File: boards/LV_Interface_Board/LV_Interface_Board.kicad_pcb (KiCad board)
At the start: 2 copper layers, 136 x 100 mm, 23 parts, among them J1 Ampseal_35, J2 Ampseal_35, J3 micromatch_male_6, J4 micromatch_male_20, J5 micromatch_male_20, J6 micromatch_male_12, J7 micromatch_male_18, J8 micromatch_male_20, J9 micromatch_male_20, SW1 3P4T_rotary_switch, U1 RJ45_VT, U2 HT16K33

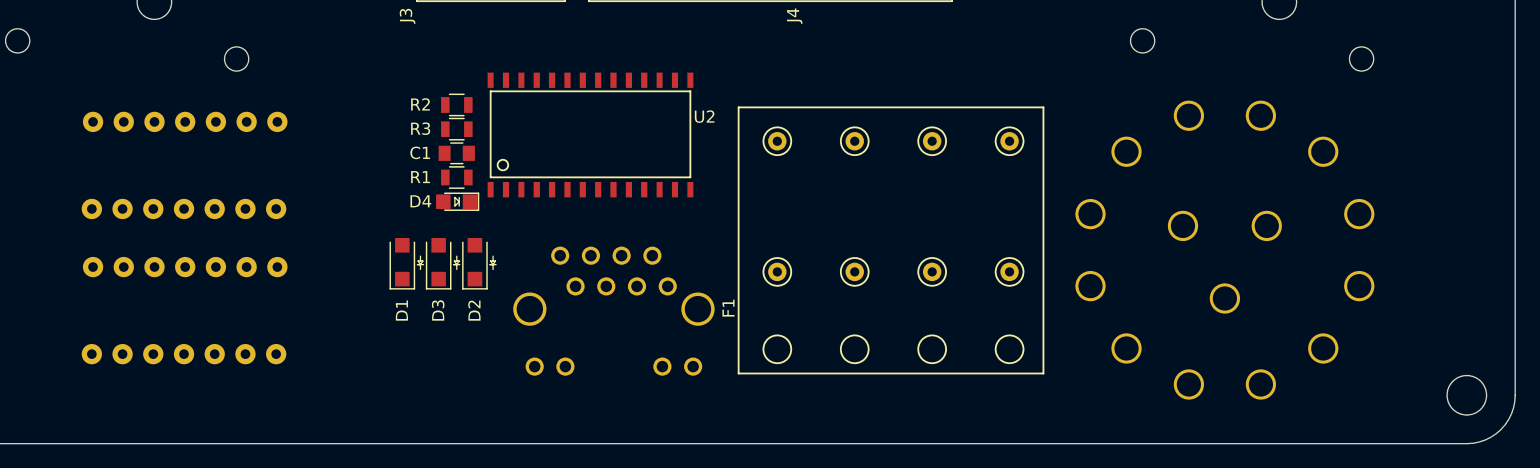
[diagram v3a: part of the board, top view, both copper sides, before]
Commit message: updated layout based on CAD interferences
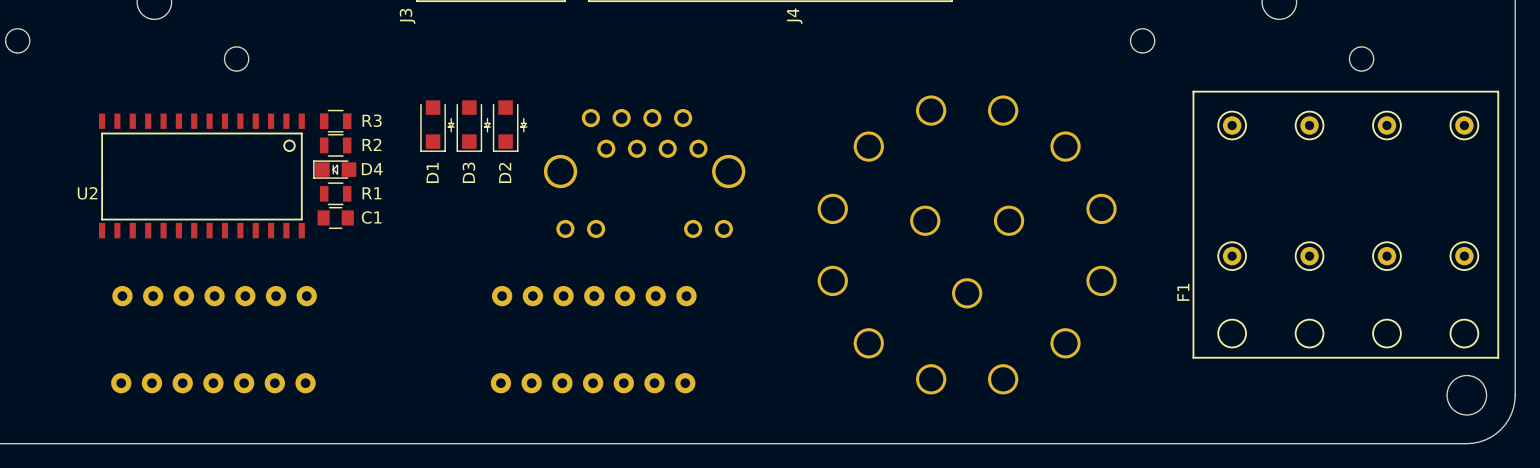
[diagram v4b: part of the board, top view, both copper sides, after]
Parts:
- moved F1 37.6 mm to (139.6, 140.9)
- moved LED1 33.9 mm to (86.8, 141.4)
- moved SW1 21.3 mm to (117.7, 133.6)
- moved U2 16.6 mm to (62.7, 123.3), turned to 180 degrees
- moved LED2 14.6 mm to (55.4, 141.4)
- moved D1 11.7 mm to (73.5, 123.6)
- moved D2 11.7 mm to (79.5, 123.6)
- moved D3 11.7 mm to (76.5, 123.6)
- moved U1 11.7 mm to (97.6, 132.3)
- moved C1 11.3 mm to (65.5, 131.3), turned to 180 degrees
- moved R2 10.6 mm to (65.5, 125.3), turned to 180 degrees
- moved D4 10.4 mm to (65.5, 127.3), turned to 0 degrees
- moved R1 10.1 mm to (65.5, 129.3), turned to 180 degrees
- moved R3 10.0 mm to (65.5, 123.3), turned to 180 degrees

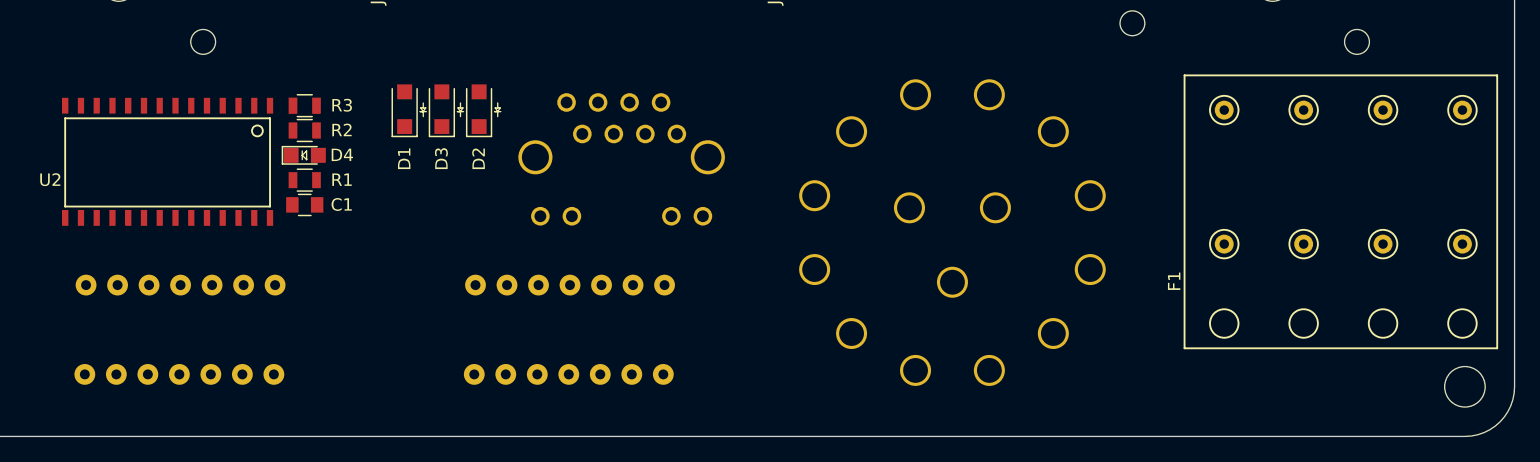
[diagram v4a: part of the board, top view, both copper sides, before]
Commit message: finished CAD, fixed fuse block footprint
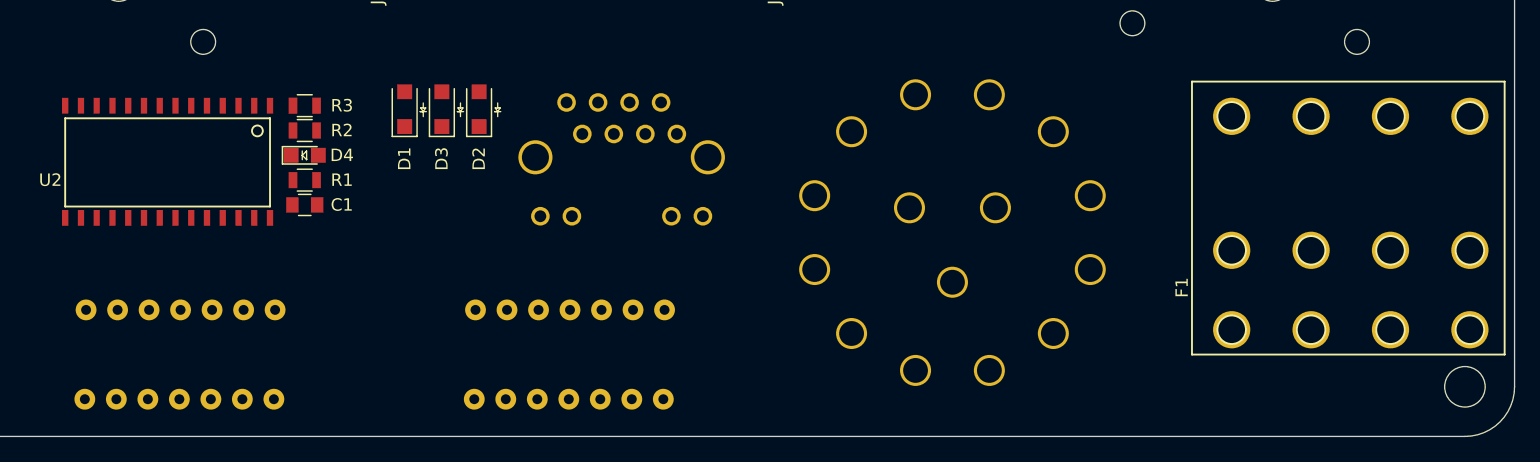
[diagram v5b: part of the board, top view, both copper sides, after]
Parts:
- moved LED1 2.00 mm to (86.8, 143.4)
- moved LED2 2.00 mm to (55.4, 143.4)
- moved F1 0.78 mm to (140.2, 141.4)
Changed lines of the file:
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@@
     (links 173)
     (no_connects 173)
-    (area 6.435716 32.3 178.564286 172.0894)
+    (area 26.949999 49.949999 163.050001 150.050001)
     (thickness 1.6)
     (drawings 34)
@@
     )
   )
-  (module footprints:fuse_block (layer F.Cu)
-    (at 139.6 140.898 90)
-    (fp_text reference F1 (at 3.4 -4 90) (layer F.SilkS)
-      (effects (font (size 1 1) (thickness 0.15)))
-    )
-    (fp_text value fuse_holder_125V_15A (at 4.4 -5.8 90) (layer F.Fab)
-      (effects (font (size 1 1) (thickness 0.15)))
-    )
-    (fp_line (start -2 22) (end -2 -3.2) (layer F.SilkS) (width 0.15))
-    (fp_line (start 20 22) (end -2 22) (layer F.SilkS) (width 0.15))
-    (fp_line (start 20 -3.2) (end 20 22) (layer F.SilkS) (width 0.15))
-    (fp_line (start -2 -3.2) (end 20 -3.2) (layer F.SilkS) (width 0.15))
-    (fp_circle (center 17.2 19.2) (end 16.05 19.2) (layer F.SilkS) (width 0.15))
-    (fp_circle (center 17.2 12.8) (end 16.05 12.8) (layer F.SilkS) (width 0.15))
-    (fp_circle (center 17.2 6.4) (end 16.05 6.4) (layer F.SilkS) (width 0.15))
-    (fp_circle (center 6.4 19.2) (end 5.25 19.2) (layer F.SilkS) (width 0.15))
-    (fp_circle (center 6.4 12.8) (end 5.25 12.8) (layer F.SilkS) (width 0.15))
-    (fp_circle (center 6.4 6.4) (end 6.4 5.25) (layer F.SilkS) (width 0.15))
-    (fp_circle (center 0 19.2) (end 0 18.05) (layer F.SilkS) (width 0.15))
-    (fp_circle (center 0 12.8) (end 0 11.65) (layer F.SilkS) (width 0.15))
-    (fp_circle (center 0 6.4) (end 0 5.25) (layer F.SilkS) (width 0.15))
-    (fp_circle (center 17.2 0) (end 16.05 0) (layer F.SilkS) (width 0.15))
-    (fp_circle (center 6.4 0) (end 5.25 0) (layer F.SilkS) (width 0.15))
-    (fp_circle (center 0 0) (end 0 1.15) (layer F.SilkS) (width 0.15))
-    (pad 1 thru_hole circle (at 6.4 0 90) (size 1.524 1.524) (drill 0.762) (layers *.Cu *.Mask F.SilkS)
-      (net 7 /GLVMS))
-    (pad 2 thru_hole circle (at 17.2 0 90) (size 1.524 1.524) (drill 0.762) (layers *.Cu *.Mask F.SilkS)
-      (net 8 /12V))
-    (pad 3 thru_hole circle (at 6.4 6.4 90) (size 1.524 1.524) (drill 0.762) (layers *.Cu *.Mask F.SilkS)
-      (net 7 /GLVMS))
-    (pad 4 thru_hole circle (at 17.2 6.4 90) (size 1.524 1.524) (drill 0.762) (layers *.Cu *.Mask F.SilkS)
-      (net 9 /COOLING_PUMP_12V_FUSED))
-    (pad 5 thru_hole circle (at 6.4 12.8 90) (size 1.524 1.524) (drill 0.762) (layers *.Cu *.Mask F.SilkS)
-      (net 7 /GLVMS))
-    (pad 6 thru_hole circle (at 17.2 12.8 90) (size 1.524 1.524) (drill 0.762) (layers *.Cu *.Mask F.SilkS)
-      (net 10 /MAIN_SHUTDOWN_FUSE))
-    (pad 7 thru_hole circle (at 6.4 19.2 90) (size 1.524 1.524) (drill 0.762) (layers *.Cu *.Mask F.SilkS)
-      (net 11 "Net-(F1-Pad7)"))
-    (pad 8 thru_hole circle (at 17.2 19.2 90) (size 1.524 1.524) (drill 0.762) (layers *.Cu *.Mask F.SilkS)
-      (net 12 "Net-(F1-Pad8)"))
-    (model /home/lucky/Desktop/Formula/OEM_Preferred_Parts/3DModels/fuse_block/fuse_block.wrl
-      (at (xyz 0 0 0))
-      (scale (xyz 1 1 1))
-      (rotate (xyz 0 0 0))
-    )
-  )
   (module footprints:Ampseal_35 (layer B.Cu)
     (at 143.5 56.5 270)
@@
     (pad 28 smd rect (at 0 -9.0424 180) (size 0.508 1.27) (layers F.Cu F.Paste F.Mask)
       (net 1 /5V))
+    (model /home/lucky/Desktop/Formula/OEM_Preferred_Parts/3DModels/SOP28/Document_sp.wrl
+      (at (xyz 0 0 0))
+      (scale (xyz 1 1 1))
+      (rotate (xyz 0 0 0))
+    )
   )
   (module footprints:SEGMENT_BICOL_BL-AR12Z3010 (layer B.Cu)
-    (at 86.81974 141.40082 270)
+    (at 86.81974 143.40082 270)
     (descr "SOUCE: HTTP://WWW.BETLUX.COM/PRODUCT/LED_LIGHT_BAR/BL-AR12B3010XX.PDF")
     (tags "SOUCE: HTTP://WWW.BETLUX.COM/PRODUCT/LED_LIGHT_BAR/BL-AR12B3010XX.PDF")
@@
     (pad 14 thru_hole circle (at 3.59918 7.66826 270) (size 1.6764 1.6764) (drill 0.79756) (layers *.Cu *.Paste *.Mask)
       (net 93 /COM0))
+    (model /home/lucky/Desktop/Formula/OEM_Preferred_Parts/3DModels/SEGMENT_BICOL_BL-AR12Z3010/led_bar.wrl
+      (at (xyz 0 0 0))
+      (scale (xyz 1 1 1))
+      (rotate (xyz 0 0 0))
+    )
   )
   (module footprints:SEGMENT_BICOL_BL-AR12Z3010 (layer B.Cu)
-    (at 55.4308 141.40082 270)
+    (at 55.4308 143.40082 270)
     (descr "SOUCE: HTTP://WWW.BETLUX.COM/PRODUCT/LED_LIGHT_BAR/BL-AR12B3010XX.PDF")
     (tags "SOUCE: HTTP://WWW.BETLUX.COM/PRODUCT/LED_LIGHT_BAR/BL-AR12B3010XX.PDF")
@@
     (pad 14 thru_hole circle (at 3.59918 7.66826 270) (size 1.6764 1.6764) (drill 0.79756) (layers *.Cu *.Paste *.Mask)
       (net 93 /COM0))
+    (model /home/lucky/Desktop/Formula/OEM_Preferred_Parts/3DModels/SEGMENT_BICOL_BL-AR12Z3010/led_bar.wrl
+      (at (xyz 0 0 0))
+      (scale (xyz 1 1 1))
+      (rotate (xyz 0 0 0))
+    )
+  )
+  (module footprints:fuse_block (layer F.Cu)
+    (at 140.2 141.4 90)
+    (fp_text reference F1 (at 3.4 -4 90) (layer F.SilkS)
+      (effects (font (size 1 1) (thickness 0.15)))
+    )
+    (fp_text value fuse_holder_125V_15A (at 4.4 -5.8 90) (layer F.Fab)
+      (effects (font (size 1 1) (thickness 0.15)))
+    )
+    (fp_line (start -2 22) (end -2 -3.2) (layer F.SilkS) (width 0.15))
+    (fp_line (start 20 22) (end -2 22) (layer F.SilkS) (width 0.15))
+    (fp_line (start 20 -3.2) (end 20 22) (layer F.SilkS) (width 0.15))
+    (fp_line (start -2 -3.2) (end 20 -3.2) (layer F.SilkS) (width 0.15))
+    (fp_circle (center 17.2 19.2) (end 16.05 19.2) (layer F.SilkS) (width 0.15))
+    (fp_circle (center 17.2 12.8) (end 16.05 12.8) (layer F.SilkS) (width 0.15))
+    (fp_circle (center 17.2 6.4) (end 16.05 6.4) (layer F.SilkS) (width 0.15))
+    (fp_circle (center 6.4 19.2) (end 5.25 19.2) (layer F.SilkS) (width 0.15))
+    (fp_circle (center 6.4 12.8) (end 5.25 12.8) (layer F.SilkS) (width 0.15))
+    (fp_circle (center 6.4 6.4) (end 6.4 5.25) (layer F.SilkS) (width 0.15))
+    (fp_circle (center 0 19.2) (end 0 18.05) (layer F.SilkS) (width 0.15))
+    (fp_circle (center 0 12.8) (end 0 11.65) (layer F.SilkS) (width 0.15))
+    (fp_circle (center 0 6.4) (end 0 5.25) (layer F.SilkS) (width 0.15))
+    (fp_circle (center 17.2 0) (end 16.05 0) (layer F.SilkS) (width 0.15))
+    (fp_circle (center 6.4 0) (end 5.25 0) (layer F.SilkS) (width 0.15))
+    (fp_circle (center 0 0) (end 0 1.15) (layer F.SilkS) (width 0.15))
+    (pad 1 thru_hole circle (at 6.4 0 90) (size 3 3) (drill 2.3) (layers *.Cu *.Mask F.SilkS)
+      (net 7 /GLVMS))
+    (pad 2 thru_hole circle (at 17.2 0 90) (size 3 3) (drill 2.3) (layers *.Cu *.Mask F.SilkS)
+      (net 8 /12V))
+    (pad 3 thru_hole circle (at 6.4 6.4 90) (size 3 3) (drill 2.3) (layers *.Cu *.Mask F.SilkS)
+      (net 7 /GLVMS))
+    (pad 4 thru_hole circle (at 17.2 6.4 90) (size 3 3) (drill 2.3) (layers *.Cu *.Mask F.SilkS)
+      (net 9 /COOLING_PUMP_12V_FUSED))
+    (pad 5 thru_hole circle (at 6.4 12.8 90) (size 3 3) (drill 2.3) (layers *.Cu *.Mask F.SilkS)
+      (net 7 /GLVMS))
+    (pad 6 thru_hole circle (at 17.2 12.8 90) (size 3 3) (drill 2.3) (layers *.Cu *.Mask F.SilkS)
+      (net 10 /MAIN_SHUTDOWN_FUSE))
+    (pad 7 thru_hole circle (at 6.4 19.2 90) (size 3 3) (drill 2.3) (layers *.Cu *.Mask F.SilkS)
+      (net 11 "Net-(F1-Pad7)"))
+    (pad 8 thru_hole circle (at 17.2 19.2 90) (size 3 3) (drill 2.3) (layers *.Cu *.Mask F.SilkS)
+      (net 12 "Net-(F1-Pad8)"))
+    (pad 9 thru_hole circle (at 0 0 90) (size 3 3) (drill 2.3) (layers *.Cu *.Mask F.SilkS))
+    (pad 10 thru_hole circle (at 0 6.4 90) (size 3 3) (drill 2.3) (layers *.Cu *.Mask F.SilkS))
+    (pad 11 thru_hole circle (at 0 12.8 90) (size 3 3) (drill 2.3) (layers *.Cu *.Mask F.SilkS))
+    (pad 12 thru_hole circle (at 0 19.2 90) (size 3 3) (drill 2.3) (layers *.Cu *.Mask F.SilkS))
   )
   (gr_circle (center 31 146) (end 32.63195 146) (layer Edge.Cuts) (width 0.1))

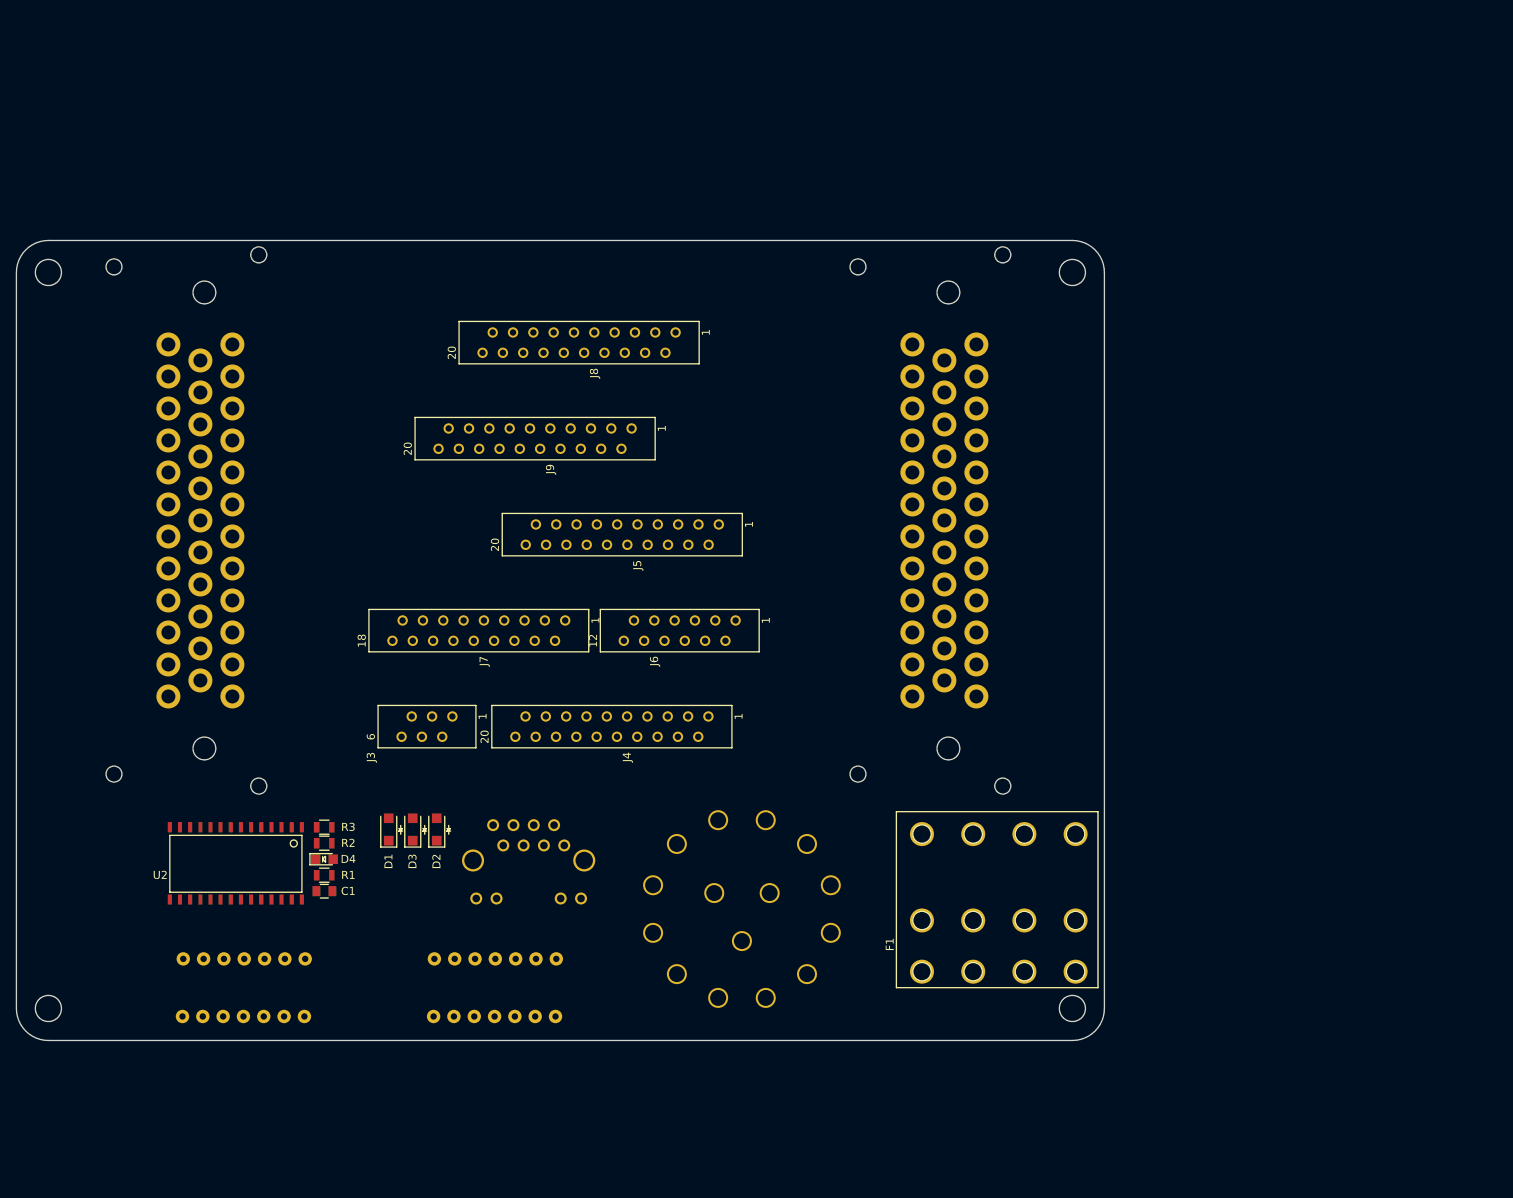
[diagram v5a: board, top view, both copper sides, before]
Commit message: first pass at routing power and CAN
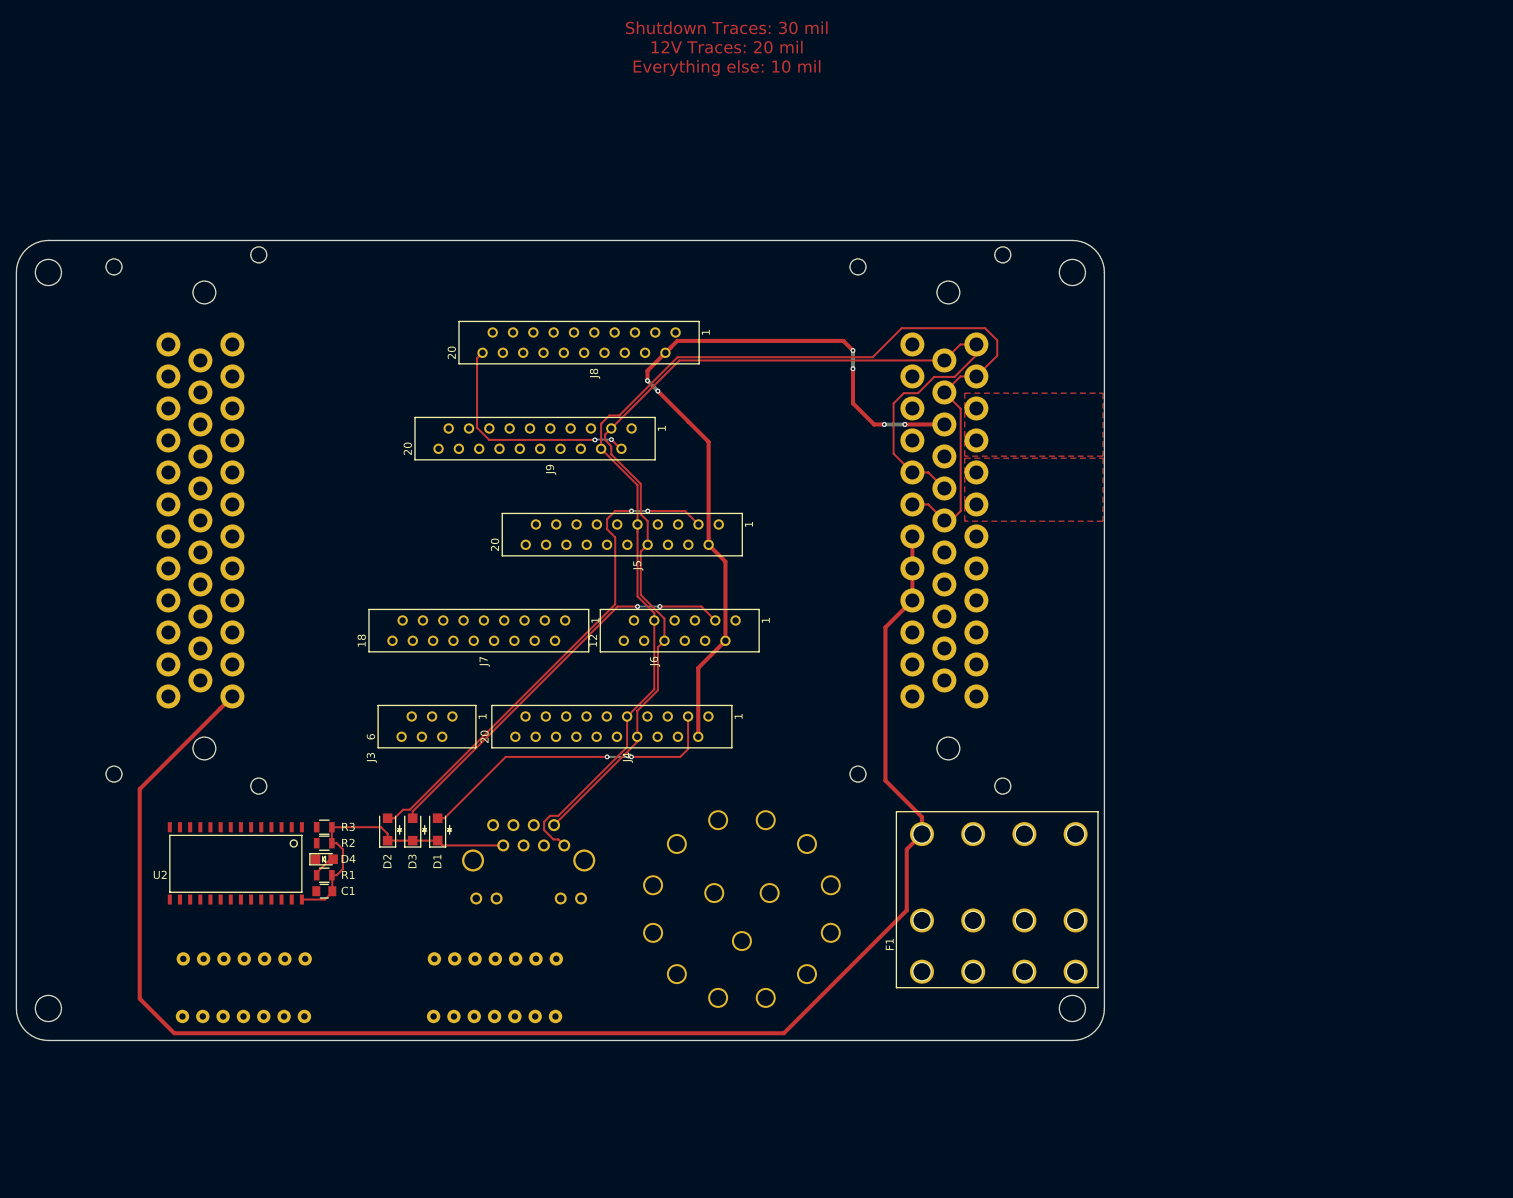
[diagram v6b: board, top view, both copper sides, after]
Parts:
- moved D2 6.13 mm to (73.4, 123.6)
- moved D1 6.11 mm to (79.7, 123.6)
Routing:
- net /12V: track 0.00 -> 295.5 mm, vias 0 -> 6
- net /CAN_LOW: track 0.00 -> 151.7 mm
- net /CAN_HIGH: track 0.00 -> 138.0 mm
- net Net-(D2-Pad2): track 0.00 -> 63.1 mm, vias 0 -> 2
- net Net-(D3-Pad2): track 0.00 -> 50.0 mm, vias 0 -> 2
- net Net-(D1-Pad2): track 0.00 -> 39.0 mm, vias 0 -> 2
- net /5V: track 0.00 -> 37.0 mm
- net /5V_DATA: track 0.00 -> 28.8 mm, vias 0 -> 2
- net Net-(D4-Pad2): track 0.00 -> 3.05 mm
- added copper zone on F.Cu, net /BAT+
- added copper zone on F.Cu, net /BREAKER
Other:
- board text added: "Shutdown Traces: 30 mil 12V Traces: 20 mil Everything else: 10 mil"
